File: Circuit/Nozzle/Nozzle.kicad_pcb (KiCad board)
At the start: 2 copper layers, 70 x 83.2 mm, 20 parts, among them J1 Coil Power, J2 CoilSignal, Q1 RFP30N06LE, U1 PC817

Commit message: [Circuit] Add distribution module to power subsystem
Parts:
- J1: footprint TerminalBlock:TerminalBlock_bornier-2_P5.08mm -> Connector_JST:JST_XH_B2B-XH-A_1x02_P2.50mm_Vertical
- moved J1 1.27 mm to (71.1, 40.6)
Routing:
- net /CoilPower+: track 3.81 -> 5.08 mm
- net /CoilPower-: track 58.0 -> 58.6 mm
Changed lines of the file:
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@@
     (thickness 1.6)
     (drawings 6)
-    (tracks 56)
+    (tracks 58)
     (zones 0)
     (modules 20)
@@
     (add_net "Net-(R3-Pad1)")
     (add_net "Net-(R4-Pad2)")
+  )
+  (module Connector_JST:JST_XH_B2B-XH-A_1x02_P2.50mm_Vertical (layer F.Cu)
+    (at 71.12 40.64)
+    (descr "JST XH series connector, B2B-XH-A (http://www.jst-mfg.com/product/pdf/eng/eXH.pdf), generated with kicad-footprint-generator")
+    (tags "connector JST XH vertical")
+    (fp_text reference J1 (at 1.25 -3.55) (layer F.SilkS)
+      (effects (font (size 1 1) (thickness 0.15)))
+    )
+    (fp_text value "Coil Power" (at 1.25 4.6) (layer F.Fab)
+      (effects (font (size 1 1) (thickness 0.15)))
+    )
+    (fp_text user %R (at 1.25 2.7) (layer F.Fab)
+      (effects (font (size 1 1) (thickness 0.15)))
+    )
+    (fp_line (start -2.85 -2.75) (end -2.85 -1.5) (layer F.SilkS) (width 0.12))
+    (fp_line (start -1.6 -2.75) (end -2.85 -2.75) (layer F.SilkS) (width 0.12))
+    (fp_line (start 4.3 2.75) (end 1.25 2.75) (layer F.SilkS) (width 0.12))
+    (fp_line (start 4.3 -0.2) (end 4.3 2.75) (layer F.SilkS) (width 0.12))
+    (fp_line (start 5.05 -0.2) (end 4.3 -0.2) (layer F.SilkS) (width 0.12))
+    (fp_line (start -1.8 2.75) (end 1.25 2.75) (layer F.SilkS) (width 0.12))
+    (fp_line (start -1.8 -0.2) (end -1.8 2.75) (layer F.SilkS) (width 0.12))
+    (fp_line (start -2.55 -0.2) (end -1.8 -0.2) (layer F.SilkS) (width 0.12))
+    (fp_line (start 5.05 -2.45) (end 3.25 -2.45) (layer F.SilkS) (width 0.12))
+    (fp_line (start 5.05 -1.7) (end 5.05 -2.45) (layer F.SilkS) (width 0.12))
+    (fp_line (start 3.25 -1.7) (end 5.05 -1.7) (layer F.SilkS) (width 0.12))
+    (fp_line (start 3.25 -2.45) (end 3.25 -1.7) (layer F.SilkS) (width 0.12))
+    (fp_line (start -0.75 -2.45) (end -2.55 -2.45) (layer F.SilkS) (width 0.12))
+    (fp_line (start -0.75 -1.7) (end -0.75 -2.45) (layer F.SilkS) (width 0.12))
+    (fp_line (start -2.55 -1.7) (end -0.75 -1.7) (layer F.SilkS) (width 0.12))
+    (fp_line (start -2.55 -2.45) (end -2.55 -1.7) (layer F.SilkS) (width 0.12))
+    (fp_line (start 1.75 -2.45) (end 0.75 -2.45) (layer F.SilkS) (width 0.12))
+    (fp_line (start 1.75 -1.7) (end 1.75 -2.45) (layer F.SilkS) (width 0.12))
+    (fp_line (start 0.75 -1.7) (end 1.75 -1.7) (layer F.SilkS) (width 0.12))
+    (fp_line (start 0.75 -2.45) (end 0.75 -1.7) (layer F.SilkS) (width 0.12))
+    (fp_line (start 0 -1.35) (end 0.625 -2.35) (layer F.Fab) (width 0.1))
+    (fp_line (start -0.625 -2.35) (end 0 -1.35) (layer F.Fab) (width 0.1))
+    (fp_line (start 5.45 -2.85) (end -2.95 -2.85) (layer F.CrtYd) (width 0.05))
+    (fp_line (start 5.45 3.9) (end 5.45 -2.85) (layer F.CrtYd) (width 0.05))
+    (fp_line (start -2.95 3.9) (end 5.45 3.9) (layer F.CrtYd) (width 0.05))
+    (fp_line (start -2.95 -2.85) (end -2.95 3.9) (layer F.CrtYd) (width 0.05))
+    (fp_line (start 5.06 -2.46) (end -2.56 -2.46) (layer F.SilkS) (width 0.12))
+    (fp_line (start 5.06 3.51) (end 5.06 -2.46) (layer F.SilkS) (width 0.12))
+    (fp_line (start -2.56 3.51) (end 5.06 3.51) (layer F.SilkS) (width 0.12))
+    (fp_line (start -2.56 -2.46) (end -2.56 3.51) (layer F.SilkS) (width 0.12))
+    (fp_line (start 4.95 -2.35) (end -2.45 -2.35) (layer F.Fab) (width 0.1))
+    (fp_line (start 4.95 3.4) (end 4.95 -2.35) (layer F.Fab) (width 0.1))
+    (fp_line (start -2.45 3.4) (end 4.95 3.4) (layer F.Fab) (width 0.1))
+    (fp_line (start -2.45 -2.35) (end -2.45 3.4) (layer F.Fab) (width 0.1))
+    (pad 2 thru_hole oval (at 2.5 0) (size 1.7 2) (drill 1) (layers *.Cu *.Mask)
+      (net 2 /CoilPower-))
+    (pad 1 thru_hole roundrect (at 0 0) (size 1.7 2) (drill 1) (layers *.Cu *.Mask) (roundrect_rratio 0.147059)
+      (net 1 /CoilPower+))
+    (model ${KISYS3DMOD}/Connector_JST.3dshapes/JST_XH_B2B-XH-A_1x02_P2.50mm_Vertical.wrl
+      (at (xyz 0 0 0))
+      (scale (xyz 1 1 1))
+      (rotate (xyz 0 0 0))
+    )
   )
   (module Resistor_THT:R_Axial_DIN0207_L6.3mm_D2.5mm_P7.62mm_Horizontal (layer F.Cu)
@@
     )
   )
-  (module TerminalBlock:TerminalBlock_bornier-2_P5.08mm (layer F.Cu)
-    (at 69.85 40.64)
-    (descr "simple 2-pin terminal block, pitch 5.08mm, revamped version of bornier2")
-    (tags "terminal block bornier2")
-    (fp_text reference J1 (at 2.54 0) (layer F.SilkS)
-      (effects (font (size 1 1) (thickness 0.15)))
-    )
-    (fp_text value "Coil Power" (at 2.54 2.54) (layer F.Fab)
-      (effects (font (size 1 1) (thickness 0.15)))
-    )
-    (fp_line (start 7.79 4) (end -2.71 4) (layer F.CrtYd) (width 0.05))
-    (fp_line (start 7.79 4) (end 7.79 -4) (layer F.CrtYd) (width 0.05))
-    (fp_line (start -2.71 -4) (end -2.71 4) (layer F.CrtYd) (width 0.05))
-    (fp_line (start -2.71 -4) (end 7.79 -4) (layer F.CrtYd) (width 0.05))
-    (fp_line (start -2.54 3.81) (end 7.62 3.81) (layer F.SilkS) (width 0.12))
-    (fp_line (start -2.54 -3.81) (end -2.54 3.81) (layer F.SilkS) (width 0.12))
-    (fp_line (start 7.62 -3.81) (end -2.54 -3.81) (layer F.SilkS) (width 0.12))
-    (fp_line (start 7.62 3.81) (end 7.62 -3.81) (layer F.SilkS) (width 0.12))
-    (fp_line (start 7.62 2.54) (end -2.54 2.54) (layer F.SilkS) (width 0.12))
-    (fp_line (start 7.54 -3.75) (end -2.46 -3.75) (layer F.Fab) (width 0.1))
-    (fp_line (start 7.54 3.75) (end 7.54 -3.75) (layer F.Fab) (width 0.1))
-    (fp_line (start -2.46 3.75) (end 7.54 3.75) (layer F.Fab) (width 0.1))
-    (fp_line (start -2.46 -3.75) (end -2.46 3.75) (layer F.Fab) (width 0.1))
-    (fp_line (start -2.41 2.55) (end 7.49 2.55) (layer F.Fab) (width 0.1))
-    (fp_text user %R (at 2.54 -2.54) (layer F.Fab)
-      (effects (font (size 1 1) (thickness 0.15)))
-    )
-    (pad 2 thru_hole circle (at 5.08 0) (size 3 3) (drill 1.52) (layers *.Cu *.Mask)
-      (net 2 /CoilPower-))
-    (pad 1 thru_hole rect (at 0 0) (size 3 3) (drill 1.52) (layers *.Cu *.Mask)
-      (net 1 /CoilPower+))
-    (model ${KISYS3DMOD}/TerminalBlock.3dshapes/TerminalBlock_bornier-2_P5.08mm.wrl
-      (offset (xyz 2.539999961853027 0 0))
-      (scale (xyz 1 1 1))
-      (rotate (xyz 0 0 0))
-    )
-  )
   (module Capacitor_THT:CP_Radial_D16.0mm_P7.50mm (layer F.Cu)
     (at 64.77 57.15 90)
@@
   (gr_line (start 110 36.83) (end 110 120) (layer Edge.Cuts) (width 0.1))
   (gr_line (start 40 36.83) (end 110 36.83) (layer Edge.Cuts) (width 0.1))
-  (segment (start 66.04 40.64) (end 69.85 40.64) (width 0.25) (layer B.Cu) (net 1))
+  (segment (start 66.04 40.64) (end 71.12 40.64) (width 0.25) (layer B.Cu) (net 1) (status 30))
   (segment (start 62.11 46.99) (end 64.77 49.65) (width 2) (layer B.Cu) (net 2) (status 20))
   (segment (start 74.93 49.53) (end 64.89 49.53) (width 2) (layer B.Cu) (net 2) (status 30))
   (segment (start 62.11 46.99) (end 51.95 46.99) (width 2) (layer B.Cu) (net 2) (status 20))
-  (segment (start 74.93 40.64) (end 74.93 49.53) (width 0.25) (layer B.Cu) (net 2) (status 30))
   (segment (start 85.09 49.53) (end 74.93 49.53) (width 2) (layer B.Cu) (net 2) (status 30))
   (segment (start 99.06 46.99) (end 95.25 46.99) (width 2) (layer B.Cu) (net 2) (status 30))
   (segment (start 95.25 46.99) (end 92.71 49.53) (width 2) (layer B.Cu) (net 2) (status 10))
   (segment (start 92.71 49.53) (end 85.09 49.53) (width 2) (layer B.Cu) (net 2) (status 20))
-  (segment (start 63.5 40.64) (end 66.04 43.18) (width 0.25) (layer B.Cu) (net 3))
-  (segment (start 58.42 40.64) (end 63.5 40.64) (width 0.25) (layer B.Cu) (net 3))
+  (segment (start 73.66 40.64) (end 74.93 41.91) (width 0.25) (layer B.Cu) (net 2) (status 10))
+  (segment (start 73.62 40.64) (end 73.66 40.64) (width 0.25) (layer B.Cu) (net 2) (status 30))
+  (segment (start 74.93 41.91) (end 74.93 49.53) (width 0.25) (layer B.Cu) (net 2) (status 20))
+  (segment (start 63.5 40.64) (end 66.04 43.18) (width 0.25) (layer B.Cu) (net 3) (status 20))
+  (segment (start 58.42 40.64) (end 63.5 40.64) (width 0.25) (layer B.Cu) (net 3) (status 10))
   (segment (start 91.44 39.37) (end 95.25 39.37) (width 0.25) (layer B.Cu) (net 4) (status 30))
   (segment (start 96.52 39.37) (end 99.06 41.91) (width 0.25) (layer B.Cu) (net 4) (status 20))

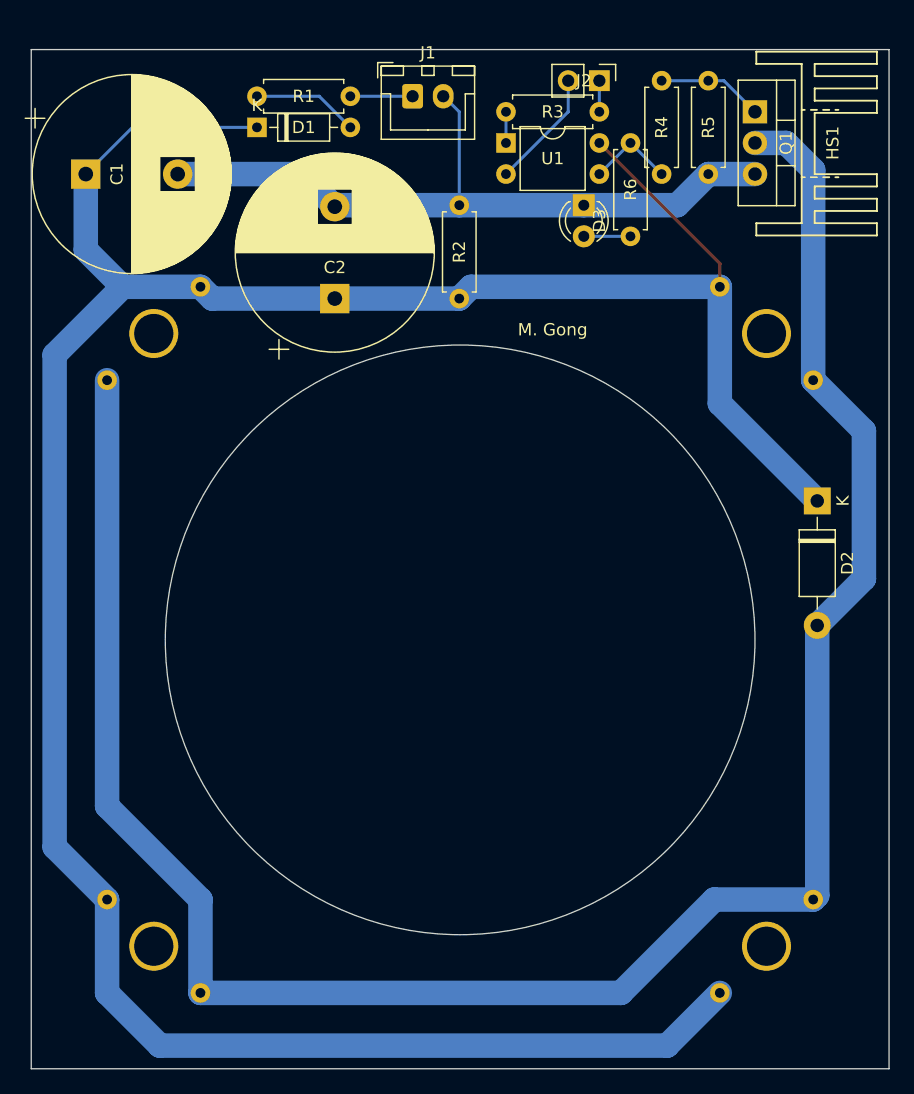
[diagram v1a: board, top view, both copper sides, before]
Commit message: [Circuit] Adjust the resistors to adapt to 5V control power
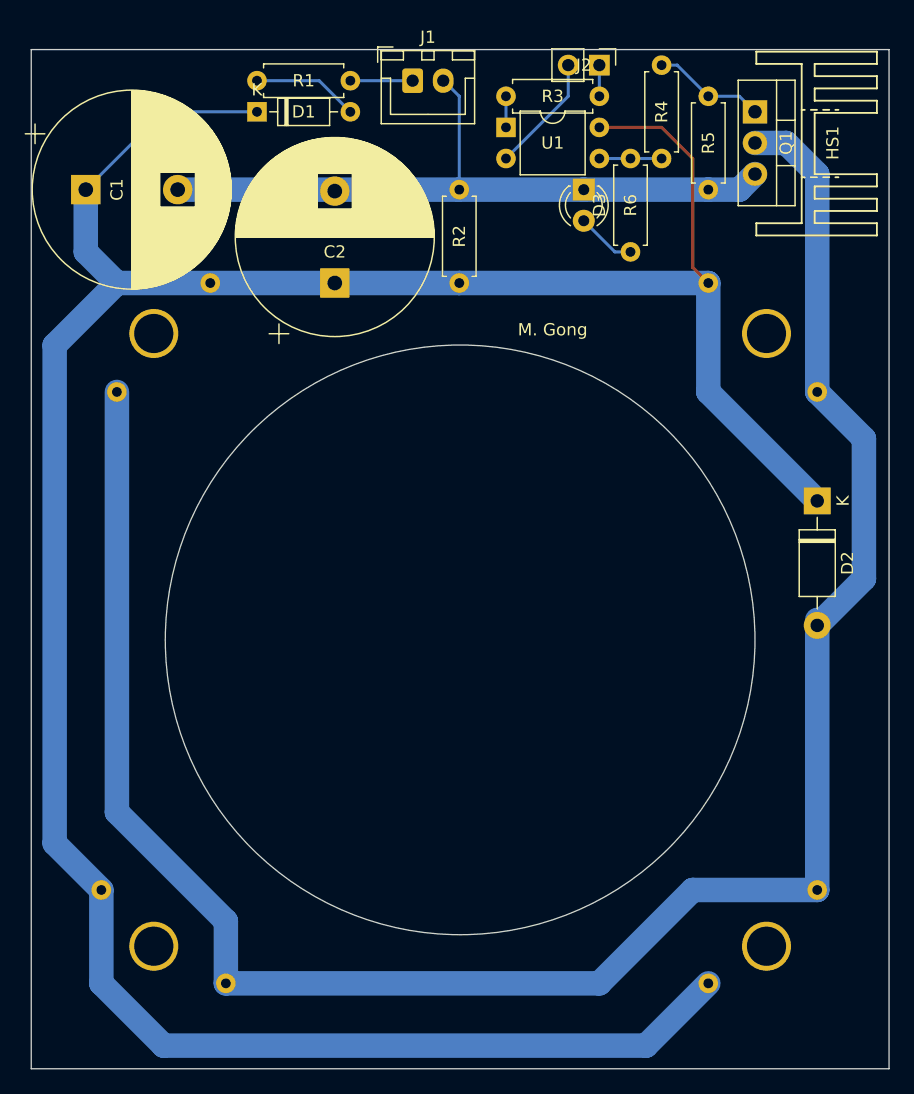
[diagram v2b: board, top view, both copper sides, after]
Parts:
- R3: value 1K -> 680
- moved D1 1.27 mm to (58.4, 41.9)
- moved D3 1.27 mm to (85.1, 48.3)
- moved J1 1.27 mm to (71.1, 39.4)
- moved R1 1.27 mm to (58.4, 39.4)
- moved R5 1.27 mm to (95.2, 40.6)
- moved U1 1.27 mm to (78.7, 43.2)
- moved C1 1.27 mm to (44.5, 48.3)
- moved C2 1.27 mm to (64.8, 55.9)
- moved J2 1.27 mm to (86.4, 38.1)
- moved R2 1.27 mm to (74.9, 55.9)
- moved R3 1.27 mm to (78.7, 40.6)
- moved R4 1.27 mm to (91.4, 38.1)
- moved R6 1.27 mm to (88.9, 45.7)
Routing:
- net Net-(D2-Pad2): track 174.9 -> 171.5 mm
- net Net-(R4-Pad2): track 7.18 -> 5.08 mm
- net /CoilPower-: track 58.6 -> 57.0 mm
- net Net-(C1-Pad1): track 227.3 -> 228.9 mm
- net Net-(D3-Pad2): track 3.81 -> 4.86 mm
- net Net-(Q1-Pad1): track 8.67 -> 9.20 mm

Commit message: [Circuit] Adjust the gate resistors
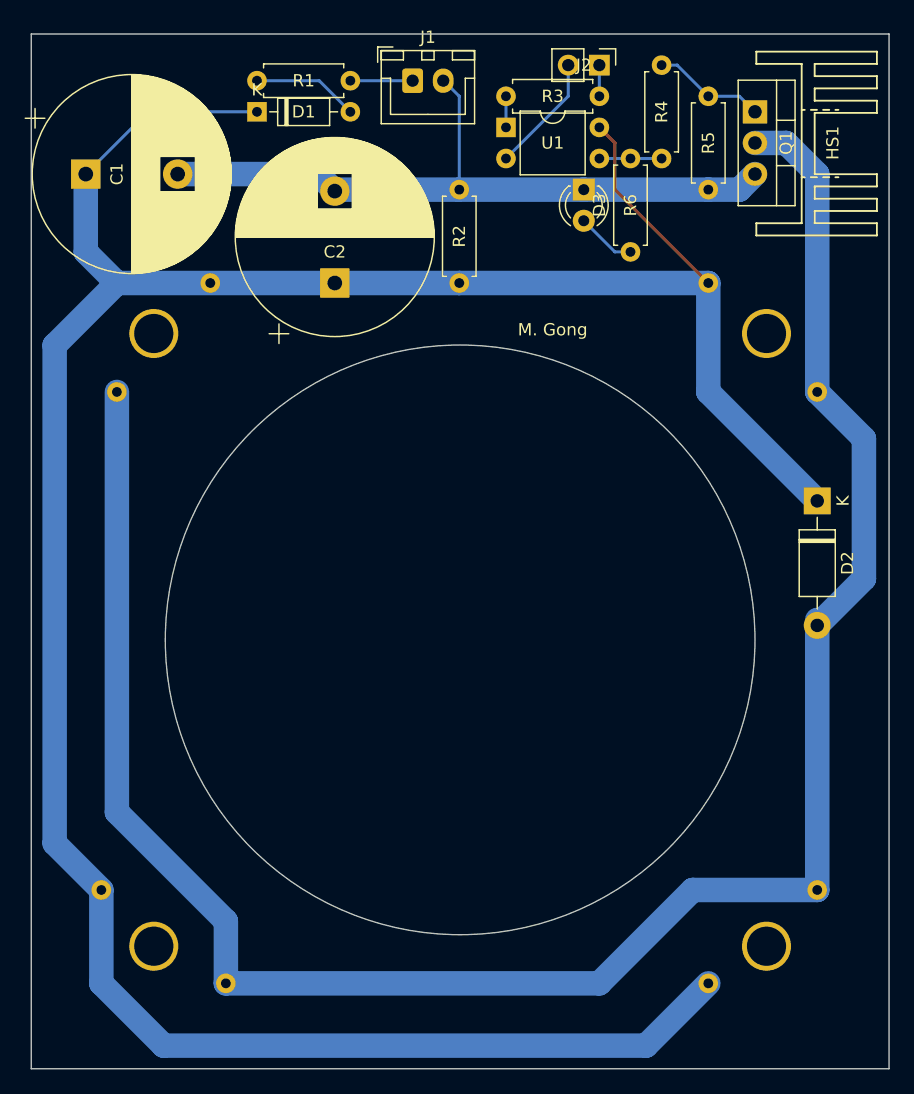
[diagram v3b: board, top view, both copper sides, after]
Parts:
- R4: value 10K -> 4.7K
- moved C1 1.27 mm to (44.5, 47.0)
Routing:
- net Net-(C1-Pad1): track 228.9 -> 226.7 mm
- net /CoilPower-: track 57.0 -> 57.7 mm
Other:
- board size 70 x 83.2 mm -> 70 x 84.4 mm
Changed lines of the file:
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@@
   )
   (setup
-    (last_trace_width 0.25)
+    (last_trace_width 2)
     (user_trace_width 2)
     (trace_clearance 0.2)
@@
       (effects (font (size 1 1) (thickness 0.15)))
     )
-    (fp_text value 10K (at 2.54 0 90) (layer F.Fab)
+    (fp_text value 4.7K (at 2.54 0 90) (layer F.Fab)
       (effects (font (size 1 1) (thickness 0.15)))
     )
@@
   )
   (module Capacitor_THT:CP_Radial_D16.0mm_P7.50mm (layer F.Cu)
-    (at 44.45 48.26)
+    (at 44.45 46.99)
     (descr "CP, Radial series, Radial, pin pitch=7.50mm, , diameter=16mm, Electrolytic Capacitor")
     (tags "CP Radial series Radial pin pitch 7.50mm  diameter 16mm Electrolytic Capacitor")
@@
   )
   (gr_circle (center 75 85) (end 99.06 85.09) (layer Edge.Cuts) (width 0.1))
-  (gr_line (start 40 120) (end 40 36.83) (layer Edge.Cuts) (width 0.1))
-  (gr_line (start 110 36.83) (end 110 120) (layer Edge.Cuts) (width 0.1))
-  (gr_line (start 40 36.83) (end 110 36.83) (layer Edge.Cuts) (width 0.1))
+  (gr_line (start 40 120) (end 40 35.56) (layer Edge.Cuts) (width 0.1))
+  (gr_line (start 110 35.56) (end 110 120) (layer Edge.Cuts) (width 0.1))
+  (gr_line (start 40 35.56) (end 110 35.56) (layer Edge.Cuts) (width 0.1))
   (segment (start 66.04 39.37) (end 71.12 39.37) (width 0.25) (layer B.Cu) (net 1) (status 30))
   (segment (start 64.89 48.26) (end 64.77 48.38) (width 2) (layer B.Cu) (net 2) (status 30))
@@
   (segment (start 73.62 39.37) (end 73.66 39.37) (width 0.25) (layer B.Cu) (net 2) (status 30))
   (segment (start 73.66 39.37) (end 74.93 40.64) (width 0.25) (layer B.Cu) (net 2) (status 10))
-  (segment (start 64.77 48.26) (end 52.07 48.26) (width 2) (layer B.Cu) (net 2) (status 30))
   (segment (start 74.93 40.64) (end 74.93 48.26) (width 0.25) (layer B.Cu) (net 2) (status 20))
   (segment (start 74.93 48.26) (end 85.09 48.26) (width 2) (layer B.Cu) (net 2) (status 30))
@@
   (segment (start 97.79 48.26) (end 99.06 46.99) (width 2) (layer B.Cu) (net 2) (status 20))
   (segment (start 95.25 48.26) (end 97.79 48.26) (width 2) (layer B.Cu) (net 2) (status 10))
+  (segment (start 63.38 46.99) (end 64.77 48.38) (width 2) (layer B.Cu) (net 2))
+  (segment (start 51.95 46.99) (end 63.38 46.99) (width 2) (layer B.Cu) (net 2))
   (segment (start 63.5 39.37) (end 66.04 41.91) (width 0.25) (layer B.Cu) (net 3) (status 20))
   (segment (start 58.42 39.37) (end 63.5 39.37) (width 0.25) (layer B.Cu) (net 3) (status 10))
@@
   (segment (start 95.25 113.03) (end 90.17 118.11) (width 2) (layer B.Cu) (net 7) (status 10))
   (segment (start 90.17 118.11) (end 50.8 118.11) (width 2) (layer B.Cu) (net 7))
-  (segment (start 50.8 41.91) (end 44.45 48.26) (width 0.25) (layer B.Cu) (net 7) (status 20))
-  (segment (start 58.42 41.91) (end 50.8 41.91) (width 0.25) (layer B.Cu) (net 7) (status 10))
   (segment (start 44.45 53.34) (end 46.99 55.88) (width 2) (layer B.Cu) (net 7))
-  (segment (start 44.45 48.26) (end 44.45 53.34) (width 2) (layer B.Cu) (net 7) (status 10))
-  (segment (start 93.98 54.61) (end 95.25 55.88) (width 0.25) (layer F.Cu) (net 7))
-  (segment (start 93.98 45.72) (end 93.98 54.61) (width 0.25) (layer F.Cu) (net 7))
-  (segment (start 91.44 43.18) (end 93.98 45.72) (width 0.25) (layer F.Cu) (net 7))
-  (segment (start 86.36 43.18) (end 91.44 43.18) (width 0.25) (layer F.Cu) (net 7))
+  (segment (start 87.63 48.26) (end 95.25 55.88) (width 0.25) (layer F.Cu) (net 7) (status 20))
+  (segment (start 86.36 43.18) (end 87.63 44.45) (width 0.25) (layer F.Cu) (net 7) (status 10))
+  (segment (start 87.63 44.45) (end 87.63 48.26) (width 0.25) (layer F.Cu) (net 7))
+  (segment (start 44.45 53.34) (end 44.45 46.99) (width 2) (layer B.Cu) (net 7))
+  (segment (start 49.53 41.91) (end 44.45 46.99) (width 0.25) (layer B.Cu) (net 7))
+  (segment (start 58.42 41.91) (end 49.53 41.91) (width 0.25) (layer B.Cu) (net 7))
   (segment (start 104.14 83.37) (end 104.14 105.41) (width 2) (layer B.Cu) (net 8) (status 30))
   (segment (start 46.99 99.06) (end 46.99 64.77) (width 2) (layer B.Cu) (net 8) (status 20))

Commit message: [Circuit] Upgrade to KiCad 6 format
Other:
- net class Default removed
